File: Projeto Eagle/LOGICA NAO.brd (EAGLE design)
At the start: 31.8 x 21.5 mm, 6 parts, among them IC1 4011D, J1 CONECTOR, J2 CONECTOR, U2 LM358D

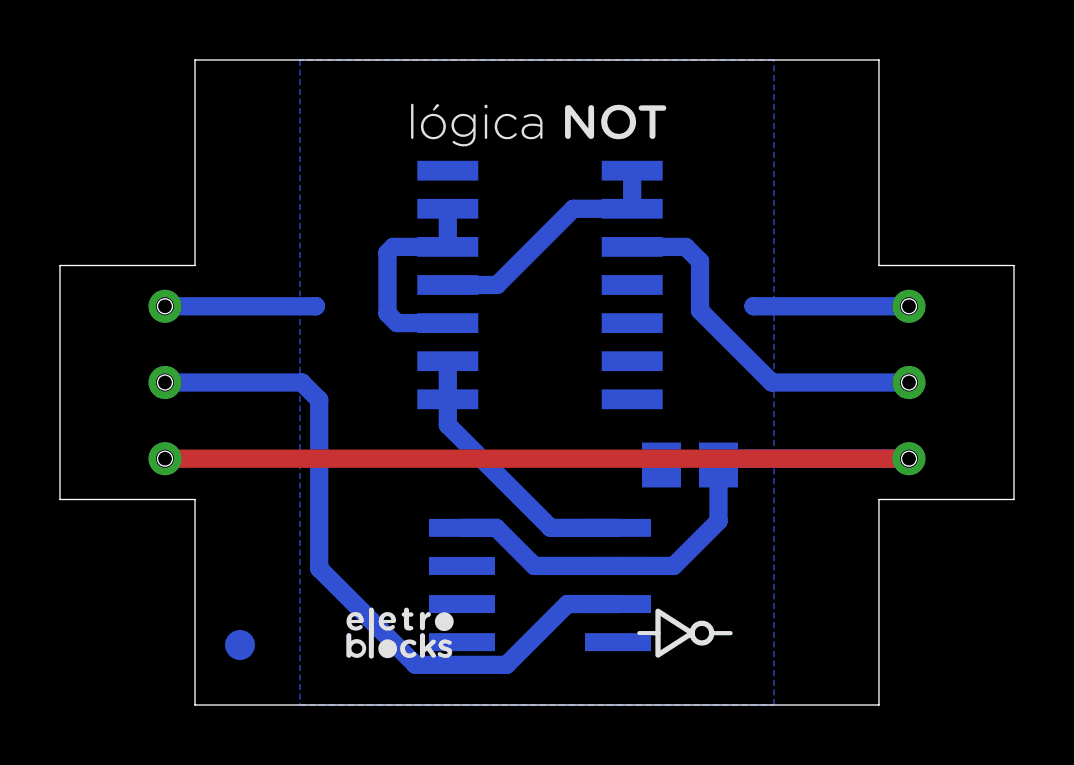
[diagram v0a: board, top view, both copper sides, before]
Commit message: correção de pads e adição de label para versionamento
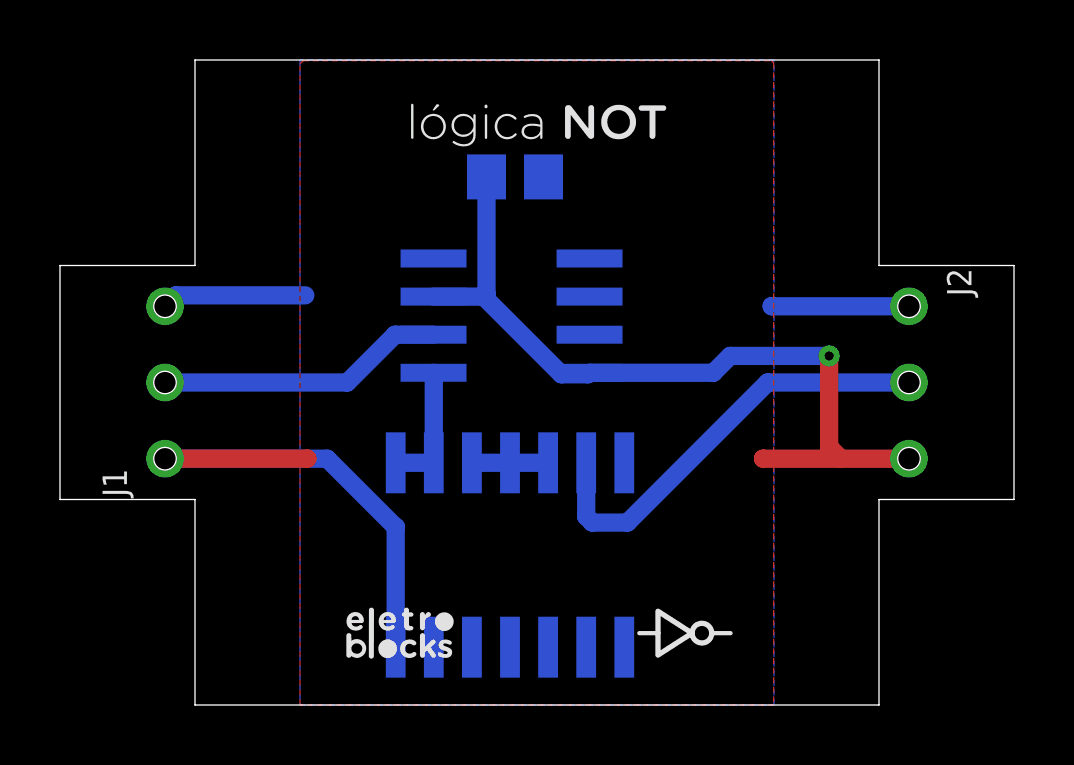
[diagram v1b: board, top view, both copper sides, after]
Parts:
- removed E$1: (no value), dicons:FIDUCIAL_G10
- removed U2: LM358D, linear:SO08
- added U1: 74HC132D, 74xx-eu:SO14
- IC1: value 4011D -> LM358D; device 40xx:SO14 -> linear:SO08
- J1: value CONECTOR -> CONECTOR_MACHO
- J2: value CONECTOR -> CONECTOR_FEMEA
- moved C1 11.2 mm to (7.17, 17.6), turned to 180 degrees
- moved IC1 1.39 mm to (7.05, 13.0)
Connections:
- removed net INVERSOR: IC1.3, IC1.5, IC1.6
- removed net N$3: IC1.1, IC1.2, U2.1
- removed net VDD: IC1.14
- removed net VSS: IC1.7
- new net VALUE: IC1.1, U1.1, U1.2
- net GND: now also IC1.4, U1.7; no longer U2.4
- net N$4: now also U1.3, U1.4, U1.5; no longer IC1.4, IC1.8, IC1.9
- net SIGNAL_IN: now also IC1.2; no longer U2.3
- net SIGNAL_OUT: now also U1.6; no longer IC1.10
- net VCC: now also IC1.3, IC1.8, U1.14; no longer U2.2, U2.8
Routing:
- net SIGNAL_IN: track 23.1 -> 9.61 mm
- net N$3: track 9.22 -> 0.00 mm
- net INVERSOR: track 7.53 -> 0.00 mm
- net N$4: track 8.47 -> 2.54 mm
- net VALUE: track 0.00 -> 4.27 mm
- net SIGNAL_OUT: track 12.1 -> 14.6 mm
- net VCC: track 43.3 -> 44.4 mm, vias 0 -> 1
- net GND: track 10.2 -> 9.42 mm
- added copper zone on layer 1, net VCC
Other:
- board text added: "V1.0.1"

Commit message: correção de sensibilidade, reformulação de lógica, adição de plano VCC e atualização da BOM
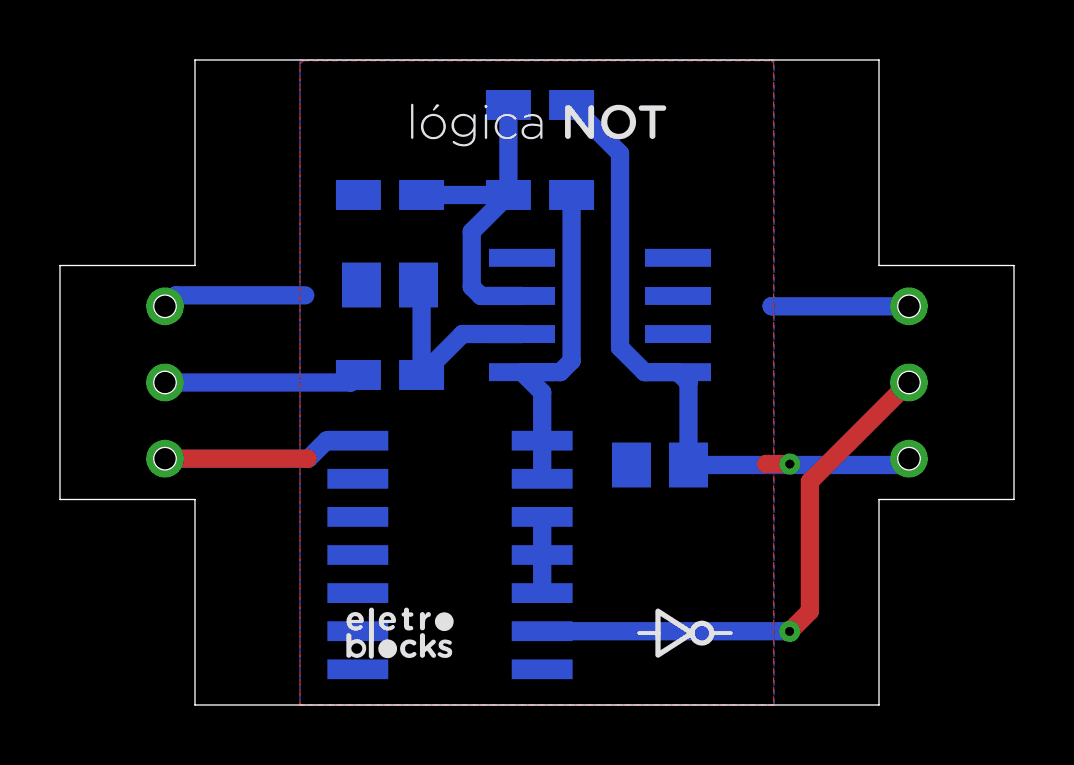
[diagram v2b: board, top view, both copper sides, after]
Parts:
- added C2: 100nF, rcl:C0805
- added R1: 2K7, rcl:R0805W
- added R2: 510R, rcl:R0805W
- added R3: 6K8, rcl:R0805W
- added R4: 10K, rcl:R0805W
- added U$1: (no value), Eletroblocks Lib:VERSAO
- moved C1 10.8 mm to (12.0, 8.00), turned to 0 degrees
- moved IC1 2.95 mm to (10.0, 13.0)
- moved U1 2.00 mm to (5.00, 5.00), turned to 270 degrees
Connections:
- new net N$3: C2.1, IC1.2, R4.2
- new net N$5: IC1.3, R1.2, R2.1, R3.1
- net GND: now also C2.2, R2.2
- net SIGNAL_IN: now also R4.1; no longer IC1.2
- net VALUE: now also R3.2
- net VCC: now also R1.1; no longer IC1.3
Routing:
- net N$5: track 0.00 -> 11.3 mm
- net VCC: track 44.4 -> 34.0 mm
- net N$3: track 0.00 -> 6.96 mm
- net VALUE: track 4.27 -> 11.2 mm
- net SIGNAL_OUT: track 14.6 -> 18.2 mm, vias 0 -> 1
- net SIGNAL_IN: track 9.61 -> 6.55 mm
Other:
- board text removed: "V1.0.1"

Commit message: correção de label
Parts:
- removed U$1: (no value), Eletroblocks Lib:VERSAO
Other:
- board text added: "V1.0.1"
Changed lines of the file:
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@@
 <vertex x="13.6948375" y="2.3306125"/>
 </polygon>
+<text x="-0.42671875" y="21.336" size="0.6096" layer="22" font="fixed" rot="MR270">V1.0.1</text>
 </plain>
 <attributes>
@@
 <attribute name="VALUE" x="4.27" y="11.46" size="1.27" layer="28" rot="MR0"/>
 </element>
-<element name="U$1" library="Eletroblocks Lib" package="VERSAO" value="" x="-2.631440625" y="21.26488125" smashed="yes" rot="R90"/>
 </elements>
 <signals>
